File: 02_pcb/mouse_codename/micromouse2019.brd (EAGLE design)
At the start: 45 x 50 mm, 80 parts

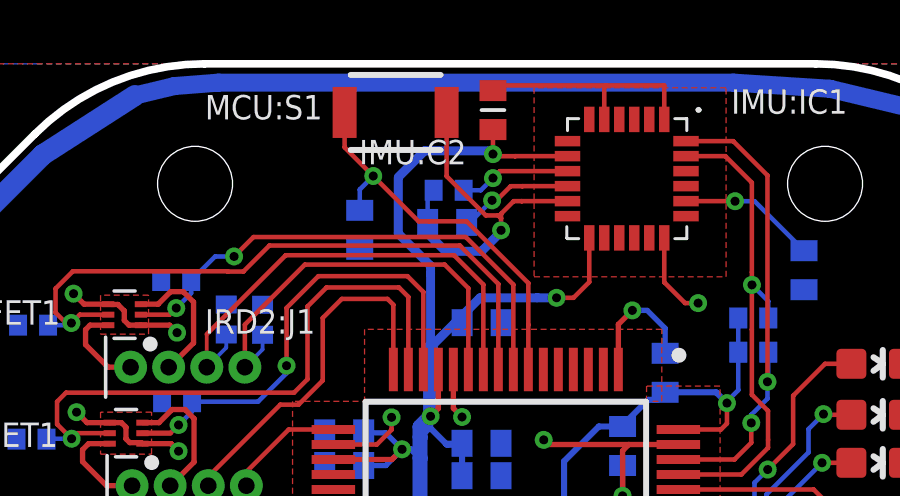
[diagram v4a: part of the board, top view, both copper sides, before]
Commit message: DRVCapacitor replaced & vias repositioned
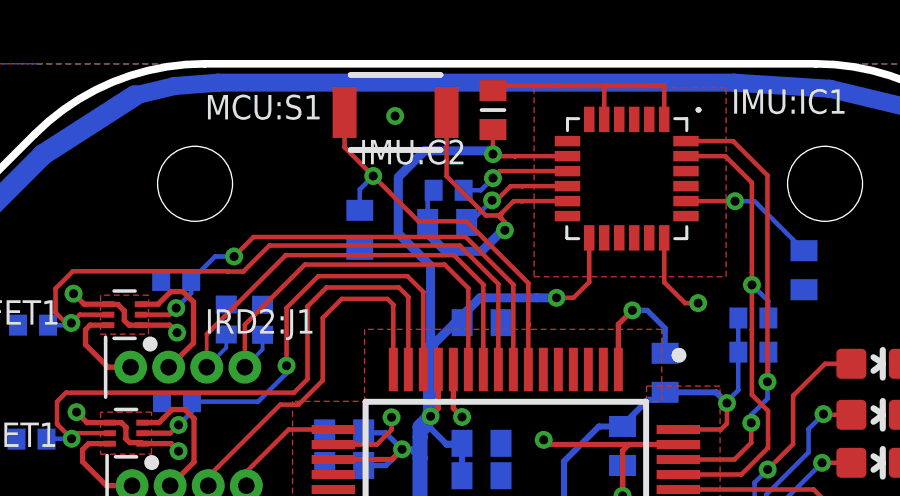
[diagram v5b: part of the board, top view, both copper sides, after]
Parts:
- MOT:C1: value 10u -> 4u7
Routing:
- net GND: track 117.3 -> 117.4 mm, vias 51 -> 52
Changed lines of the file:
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@@
 <attribute name="VALUE" x="22.9826" y="21.54" size="1.27" layer="27" rot="R90" align="top-center"/>
 </element>
-<element name="MOT:C1" library="0-micromouse2019" package="C0402" package3d_urn="urn:adsk.eagle:package:23626/2" value="10u" x="17.973" y="20.84" smashed="yes" rot="R90">
+<element name="MOT:C1" library="0-micromouse2019" package="C0402" package3d_urn="urn:adsk.eagle:package:23626/2" value="4u7" x="17.973" y="20.84" smashed="yes" rot="R90">
 <attribute name="NAME" x="21.451" y="19.751" size="0.8128" layer="25" rot="R180"/>
 <attribute name="SPICEPREFIX" value="C" x="17.973" y="20.84" size="1.778" layer="27" rot="R90" display="off"/>
@@
 <wire x1="22.892" y1="45.422" x2="22.622" y2="45.422" width="0.1524" layer="1"/>
 <wire x1="22.2" y1="45" x2="22.2" y2="44.85" width="0.1524" layer="1"/>
-<via x="22.2" y="44.45" extent="1-16" drill="0.3" diameter="0.6"/>
-<wire x1="22.2" y1="44.85" x2="22.2" y2="44.45" width="0.1524" layer="1"/>
+<via x="22.327" y="44.45" extent="1-16" drill="0.3" diameter="0.6"/>
+<wire x1="22.327" y1="44.723" x2="22.327" y2="44.45" width="0.1524" layer="1"/>
 <wire x1="22.622" y1="45.422" x2="22.2" y2="45" width="0.1524" layer="1"/>
 <wire x1="21.69238125" y1="44.94598125" x2="22.10401875" y2="44.94598125" width="0.1524" layer="1"/>
 <wire x1="22.10401875" y1="44.94598125" x2="22.2" y2="44.85" width="0.1524" layer="1"/>
+<wire x1="22.2" y1="44.85" x2="22.327" y2="44.723" width="0.1524" layer="1"/>
 <wire x1="20.385" y1="46.2533625" x2="21.69238125" y2="44.94598125" width="0.1524" layer="1"/>
 <wire x1="20.385" y1="48.379" x2="20.385" y2="46.2533625" width="0.1524" layer="1"/>
@@
 <wire x1="19.753" y1="44.347" x2="20.35" y2="43.75" width="0.3" layer="16"/>
 <wire x1="20.35" y1="43.75" x2="21.55" y2="43.75" width="0.3" layer="16"/>
-<wire x1="21.55" y1="43.75" x2="22.2" y2="44.4" width="0.3" layer="16"/>
-<wire x1="22.2" y1="44.4" x2="22.2" y2="44.45" width="0.1524" layer="16"/>
+<wire x1="21.55" y1="43.75" x2="22.25" y2="44.45" width="0.3" layer="16"/>
+<wire x1="22.25" y1="44.45" x2="22.327" y2="44.45" width="0.1524" layer="16"/>
 <contactref element="PWR:CONN1" pad="2"/>
 <wire x1="13.68" y1="0.91" x2="17.56" y2="0.91" width="0.5" layer="1"/>
@@
 <wire x1="37.808" y1="43.278" x2="37.719" y2="43.189" width="0.1524" layer="1"/>
 <wire x1="37.719" y1="43.189" x2="37.719" y2="42.672" width="0.1524" layer="1"/>
+<via x="18.669" y="48.26" extent="1-16" drill="0.3" diameter="0.6"/>
 </signal>
 <signal name="+3V3">

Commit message: minior fixes
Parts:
- moved IMU:R1 0.38 mm to (20.5, 46.2)
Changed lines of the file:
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@@
 <layer number="132" name="bAdjust" color="7" fill="1" visible="no" active="yes"/>
 <layer number="144" name="Drill_legend" color="7" fill="1" visible="no" active="yes"/>
-<layer number="150" name="Notes" color="7" fill="1" visible="no" active="yes"/>
+<layer number="150" name="Notes" color="7" fill="1" visible="yes" active="yes"/>
 <layer number="151" name="HeatSink" color="7" fill="1" visible="no" active="yes"/>
 <layer number="152" name="_bDocu" color="7" fill="1" visible="no" active="yes"/>
@@
 <attribute name="MANUFACTURER_PART_NUMBER" value="B3U-1000P" x="42.164" y="2.921" size="1.778" layer="27" rot="R45" display="off"/>
 <attribute name="MOUSER_PART_NUMBER" value="653-B3U-1000P" x="42.164" y="2.921" size="1.778" layer="27" rot="R45" display="off"/>
-<attribute name="NAME" x="40.9124125" y="4.15563125" size="0.8128" layer="25" rot="R45" align="center"/>
+<attribute name="NAME" x="42.406009375" y="5.80396875" size="0.8128" layer="25" align="center"/>
 <attribute name="VALUE" x="43.240896875" y="1.01255" size="1.27" layer="27" rot="R45" align="center"/>
 </element>
@@
 </element>
 <element name="MCU:C11" library="0-micromouse2019" package="C0402" package3d_urn="urn:adsk.eagle:package:23626/2" value="100n" x="17.49" y="44.465" smashed="yes" rot="MR270">
-<attribute name="NAME" x="16.165" y="41.387" size="0.8128" layer="26" rot="MR90"/>
+<attribute name="NAME" x="15.911" y="40.752" size="0.8128" layer="26" rot="MR90"/>
 <attribute name="SPICEPREFIX" value="C" x="98.77" y="57.165" size="1.778" layer="28" rot="MR270" display="off"/>
 <attribute name="VALUE" x="19.014" y="46.243" size="0.8128" layer="28" rot="MR270"/>
@@
 <attribute name="VALUE" x="33.824" y="44.898" size="0.8128" layer="28" rot="MR270"/>
 </element>
-<element name="IMU:R1" library="0-micromouse2019" package="R0402" package3d_urn="urn:adsk.eagle:package:23547/3" value="47k" x="20.454" y="45.785" smashed="yes" rot="MR180">
-<attribute name="NAME" x="26.022" y="45.384" size="0.8128" layer="26" rot="MR0"/>
-<attribute name="SPICEPREFIX" value="R" x="20.454" y="45.785" size="1.778" layer="28" rot="MR180" display="off"/>
-<attribute name="VALUE" x="19.819" y="47.182" size="0.8128" layer="28" rot="MR180"/>
+<element name="IMU:R1" library="0-micromouse2019" package="R0402" package3d_urn="urn:adsk.eagle:package:23547/3" value="47k" x="20.454" y="46.166" smashed="yes" rot="MR180">
+<attribute name="NAME" x="26.022" y="45.765" size="0.8128" layer="26" rot="MR0"/>
+<attribute name="SPICEPREFIX" value="R" x="20.454" y="46.166" size="1.778" layer="28" rot="MR180" display="off"/>
+<attribute name="VALUE" x="19.819" y="47.563" size="0.8128" layer="28" rot="MR180"/>
 </element>
 <element name="IMU:C4" library="0-micromouse2019" package="C0402" package3d_urn="urn:adsk.eagle:package:23626/2" value="10n" x="21.553" y="41.372" smashed="yes" rot="MR180">
@@
 </element>
 <element name="IMU:C2" library="0-micromouse2019" package="C0402" package3d_urn="urn:adsk.eagle:package:23626/2" value="100n" x="21.93" y="48.458" smashed="yes" rot="R90">
-<attribute name="NAME" x="17.47" y="46.65" size="0.8128" layer="25"/>
+<attribute name="NAME" x="21.422" y="43.505" size="0.8128" layer="25" rot="R90"/>
 <attribute name="SPICEPREFIX" value="C" x="21.93" y="48.458" size="1.778" layer="27" rot="R90" display="off"/>
 <attribute name="VALUE" x="23.835" y="47.823" size="1.27" layer="27" rot="R90"/>
@@
 </element>
 <element name="PWR:LDO2" library="0-micromouse2019" package="SON50P200X200X80-7T92X145" package3d_urn="urn:adsk.eagle:package:9227372/1" value="PS_LDL112PU" x="15.445" y="6.367" smashed="yes" rot="R180">
-<attribute name="NAME" x="16.3365" y="5.0655" size="0.8128" layer="25" rot="R180"/>
+<attribute name="NAME" x="14.0505" y="5.8275" size="0.8128" layer="25" rot="R180"/>
 </element>
 <element name="PWR:LDO1" library="0-micromouse2019" package="SON65P200X200X80-7T100X160" package3d_urn="urn:adsk.eagle:package:9228423/1" value="PS_TPS735DRVT" x="21.144" y="5.203" smashed="yes" rot="R180">
@@
 </element>
 <element name="MCU:R4" library="0-micromouse2019" package="R0402" package3d_urn="urn:adsk.eagle:package:23547/3" value="270R" x="8.8" y="10.2" smashed="yes" rot="MR0">
-<attribute name="NAME" x="14.515" y="9.819" size="0.8128" layer="26" rot="MR0"/>
+<attribute name="NAME" x="14.261" y="9.819" size="0.8128" layer="26" rot="MR0"/>
 <attribute name="SPICEPREFIX" value="R" x="8.8" y="10.2" size="1.778" layer="28" rot="MR0" display="off"/>
 <attribute name="VALUE" x="9.435" y="8.803" size="0.8128" layer="28" rot="MR0"/>
@@
 </element>
 <element name="IRD1:R5" library="0-micromouse2019" package="R0402" package3d_urn="urn:adsk.eagle:package:23547/3" value="2R" x="11.75" y="34.15" smashed="yes" rot="MR90">
-<attribute name="NAME" x="11.623" y="28.943" size="0.8128" layer="26" rot="MR90"/>
+<attribute name="NAME" x="11.824" y="32.324" size="0.8128" layer="26" rot="MR0"/>
 <attribute name="SPICEPREFIX" value="R" x="11.75" y="34.15" size="1.778" layer="28" rot="MR90" display="off"/>
 <attribute name="VALUE" x="10.353" y="33.515" size="0.8128" layer="28" rot="MR90"/>
 </element>
 <element name="IRD1:R6" library="0-micromouse2019" package="R0402" package3d_urn="urn:adsk.eagle:package:23547/3" value="2R" x="13" y="34.15" smashed="yes" rot="MR90">
-<attribute name="NAME" x="12.492" y="28.943" size="0.8128" layer="26" rot="MR90"/>
+<attribute name="NAME" x="13.703" y="34.244" size="0.8128" layer="26" rot="MR180"/>
 <attribute name="SPICEPREFIX" value="R" x="13" y="34.15" size="1.778" layer="28" rot="MR90" display="off"/>
 <attribute name="VALUE" x="11.603" y="33.515" size="0.8128" layer="28" rot="MR90"/>
@@
 <wire x1="22.162" y1="46.422" x2="21.93" y2="46.19" width="0.1524" layer="1"/>
 <via x="21.93" y="46.19" extent="1-16" drill="0.3" diameter="0.6"/>
-<wire x1="21.93" y1="46.19" x2="21.525" y2="45.785" width="0.1524" layer="16"/>
-<wire x1="21.525" y1="45.785" x2="20.954" y2="45.785" width="0.1524" layer="16"/>
+<wire x1="21.93" y1="46.19" x2="21.906" y2="46.166" width="0.1524" layer="16"/>
+<wire x1="21.906" y1="46.166" x2="20.954" y2="46.166" width="0.1524" layer="16"/>
 <wire x1="24.415" y1="46.422" x2="22.162" y2="46.422" width="0.1524" layer="1"/>
 </signal>
@@
 <wire x1="25.64" y1="49.22" x2="25.64" y2="48.147" width="0.1524" layer="1"/>
 <wire x1="27.64" y1="49.28" x2="27.64" y2="48.147" width="0.1524" layer="1"/>
-<wire x1="19.753" y1="44.712" x2="19.753" y2="45.584" width="0.1524" layer="16"/>
-<wire x1="19.753" y1="45.584" x2="19.954" y2="45.785" width="0.1524" layer="16"/>
+<wire x1="19.753" y1="44.712" x2="19.753" y2="45.965" width="0.1524" layer="16"/>
+<wire x1="19.753" y1="45.965" x2="19.954" y2="46.166" width="0.1524" layer="16"/>
 <wire x1="19.753" y1="44.712" x2="19.753" y2="44.347" width="0.1524" layer="16"/>
 <wire x1="19.753" y1="44.347" x2="20.35" y2="43.75" width="0.3" layer="16"/>
